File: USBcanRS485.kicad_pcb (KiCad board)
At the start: 2 copper layers, 68.5 x 34.5 mm, 30 parts

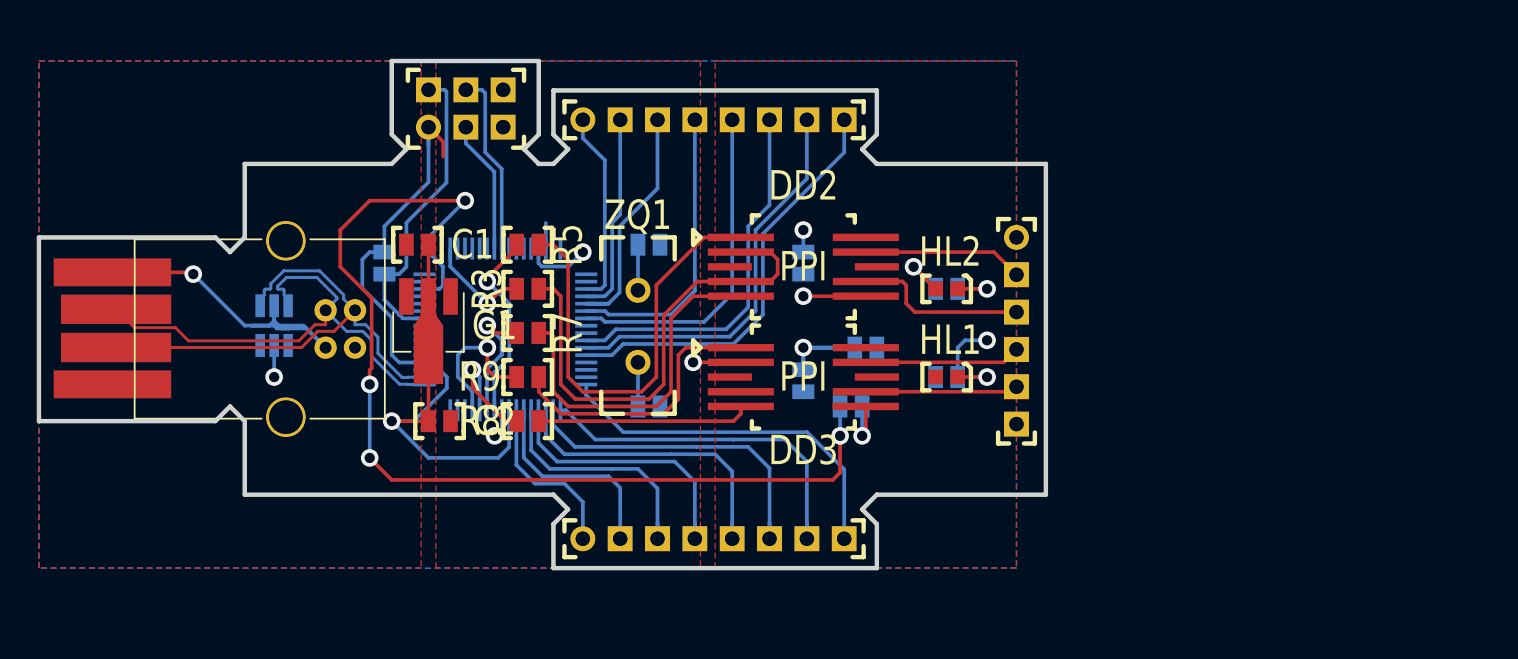
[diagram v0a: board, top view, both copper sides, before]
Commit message: Проект почти закончен
Осталось добавить предохранители на вход и выход
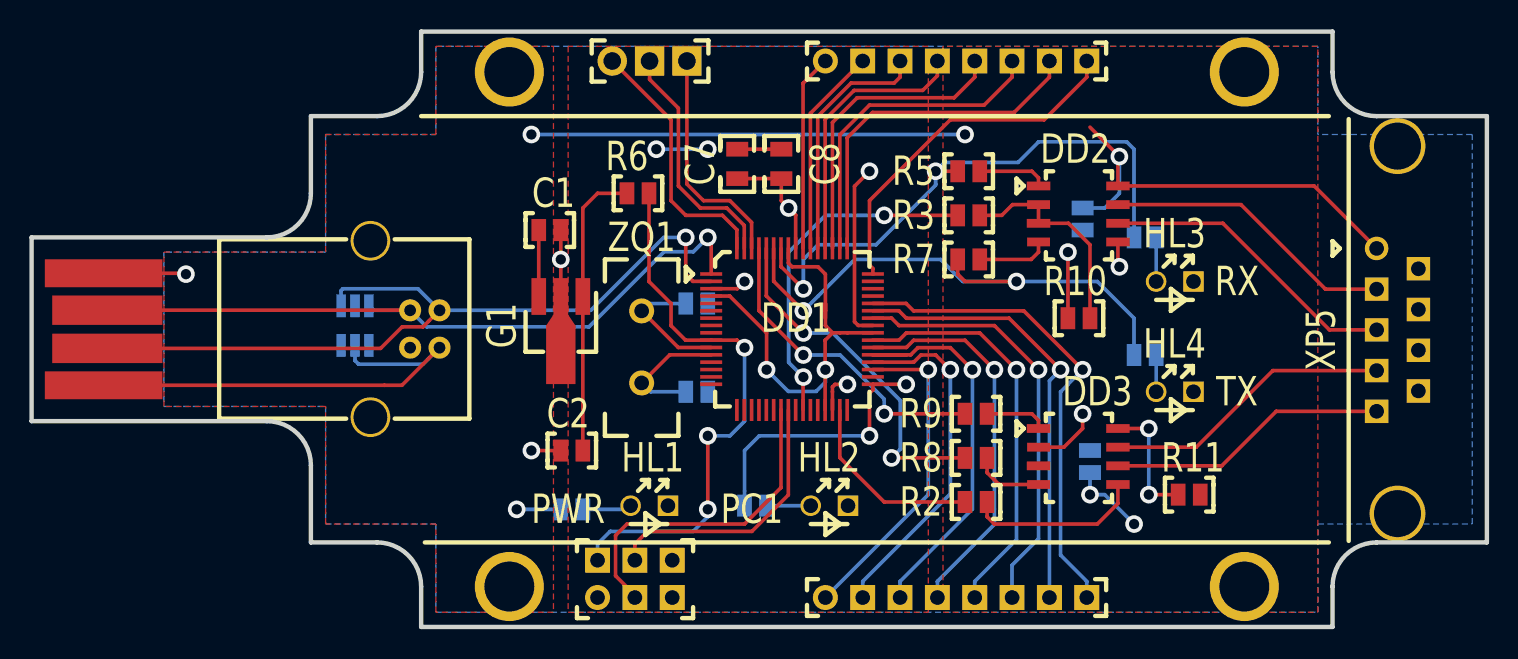
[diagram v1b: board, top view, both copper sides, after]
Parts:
- added C7: 16В-10мкФ, N_RLC:Конденсатор_SMD_0805, F.Cu at (166.0, 111.5)
- added C8: 16В-10мкФ, N_RLC:Конденсатор_SMD_0805, F.Cu at (169.0, 111.5)
- added HL3: Светодиод, N_VD_HL:LED_D3.0mm, F.Cu at (194.5, 120.5)
- added HL4: Светодиод, N_VD_HL:LED_D3.0mm, F.Cu at (194.5, 128.0)
- added R10: 20 кОм, N_RLC:Конденсатор_SMD_0603, F.Cu at (190.0, 123.0)
- added R12: 15 Ом, N_RLC:Конденсатор_SMD_0603, B.Cu at (193.0, 117.5)
- added R13: 15 Ом, N_RLC:Конденсатор_SMD_0603, B.Cu at (193.0, 125.5)
- added REF**: Корпус_G403, OTSTOINIK:Корпус_G403, F.Cu at (130.5, 148.8)
- added Ref**: icon_motor_micro, MOTOR_ICO:Знак_МОТОР_micro, B.Cu at (159.0, 112.5)
- added XP7: Вилка_СНП346-3ВП21-1-В, MOTOR_X:Вилка_СНП346-3ВП21-1-В, F.Cu at (157.5, 105.5)
- DD1, R11, R2, R6: moved to F.Cu
- DD2: value 5559ИН28У -> 5559ИН10; footprint MOTOR_DD:Микросхема_5559ИНхх -> N_DD:SO-8_RS485_CAN_Milandr_OTK
- DD3: footprint MOTOR_DD:Микросхема_5559ИНхх -> N_DD:SO-8_RS485_CAN_Milandr_OTK
- G1: footprint TO_SOT_Packages_SMD:SOT-89-3_Handsoldering -> N_DD:SOT-89-3_Handsoldering
- HL1, HL2: footprint N_VD_HL:Светодиод_SMD_0603 -> N_VD_HL:LED_D3.0mm
- VD1: footprint TO_SOT_Packages_SMD:SOT-23-6_Handsoldering -> N_DD:SOT-23-6_Handsoldering
- XP5: footprint N_X:Вилка_PLS6_вертикальная -> N_X:DSUB-9_Female_Horizontal_P2.77x2.84mm_EdgePinOffset7.70mm_Housed_MountingHolesOffset9.12mm
- XP6: footprint Connectors:USB_B -> N_X:USB_B
- moved XP3 36.4 mm to (172.0, 142.0)
- moved XP4 36.4 mm to (172.0, 105.5)
- moved XP2 34.0 mm to (156.5, 142.0)
- moved R8 30.6 mm to (181.5, 132.5)
- moved R9 30.6 mm to (181.5, 129.5)
- moved R3 30.4 mm to (182.5, 116.0)
- moved R5 30.4 mm to (181.0, 113.0)
- moved R7 30.4 mm to (181.0, 119.0)
- moved R1 25.6 mm to (155.5, 136.0), turned to 180 degrees
- moved DD1 24.9 mm to (158.5, 116.0)
- moved XP5 24.5 mm to (209.5, 118.2), turned to 90 degrees
- moved R11 22.8 mm to (196.0, 135.0), turned to 0 degrees
- moved HL1 22.5 mm to (158.8, 135.8)
- moved C6 20.7 mm to (190.0, 133.5), turned to 90 degrees
- moved DD2 20.1 mm to (186.5, 114.0)
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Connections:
- net Net-(C3-Pad2) renamed /Osc+
- net Net-(C4-Pad2) renamed /Osc-
- R2 pad 2: Net-(DD1-Pad14) -> Net-(DD1-Pad31)
- R3 pad 2: Net-(DD1-Pad17) -> Net-(DD1-Pad26)
- R4 pad 2: Net-(DD1-Pad34) -> Net-(DD1-Pad33)
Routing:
- net 5В: track 17.6 -> 103.3 mm, vias 4 -> 6
- net Net-(DD1-Pad14): track 71.5 -> 0.00 mm, vias 4 -> 0
- net Net-(DD1-Pad59): track 9.33 -> 38.4 mm, vias 1 -> 2
- net Net-(DD1-Pad58): track 13.2 -> 39.5 mm, vias 1 -> 2
- net 3B: track 31.3 -> 57.2 mm, vias 2 -> 4
- net U2RX: track 30.6 -> 4.74 mm
- net Net-(DD1-Pad26): track 0.00 -> 23.7 mm, vias 0 -> 2
- net D-: track 34.5 -> 55.3 mm, vias 0 -> 1
- net U2TX: track 24.1 -> 4.90 mm
- net Net-(DD1-Pad33): track 0.00 -> 18.5 mm, vias 0 -> 2
- net PE1-RSen: track 32.9 -> 14.7 mm
- net Net-(DD1-Pad64): track 0.00 -> 17.7 mm
- net RESET: track 21.0 -> 38.0 mm, vias 0 -> 3
- net Net-(DD1-Pad63): track 0.00 -> 16.5 mm
- net Net-(DD1-Pad60): track 8.14 -> 24.5 mm, vias 1 -> 2
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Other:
- board size 68.5 x 34.5 mm -> 99 x 40.5 mm
- board text added: "1268-4010-001"
- board text added: "PC1"
- board text added: "PWR"
- board text added: "RX"
- board text added: "TX"

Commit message: Доработка проекта
Плата приведена к размерам корпуса G403. Добавлены предохранители.
Привязаны актуальные 3D-модели.
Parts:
- added FU1: Предохранитель, N_VD_HL:Fuse_1812, F.Cu at (141.5, 112.5)
- added FU2: Предохранитель, N_VD_HL:Fuse_1812, F.Cu at (201.0, 112.5)
- XP5: footprint N_X:DSUB-9_Female_Horizontal_P2.77x2.84mm_EdgePinOffset7.70mm_Housed_MountingHolesOffset9.12mm -> N_X:DSUB-9_Female
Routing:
- net GND: track 52.2 -> 73.3 mm, vias 10 -> 11
- net 5В: track 103.3 -> 115.0 mm
- net 3B: track 57.2 -> 62.9 mm
